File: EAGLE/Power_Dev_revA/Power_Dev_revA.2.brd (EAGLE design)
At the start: 63.5 x 31.8 mm, 36 parts, among them J5 MICRO_USB_SMD, Q1 SI2301CDS-T1-GE3, Q2 SI2301CDS-T1-GE3, U1 CN3791, U2 DW01A-G, U4 FS8205A

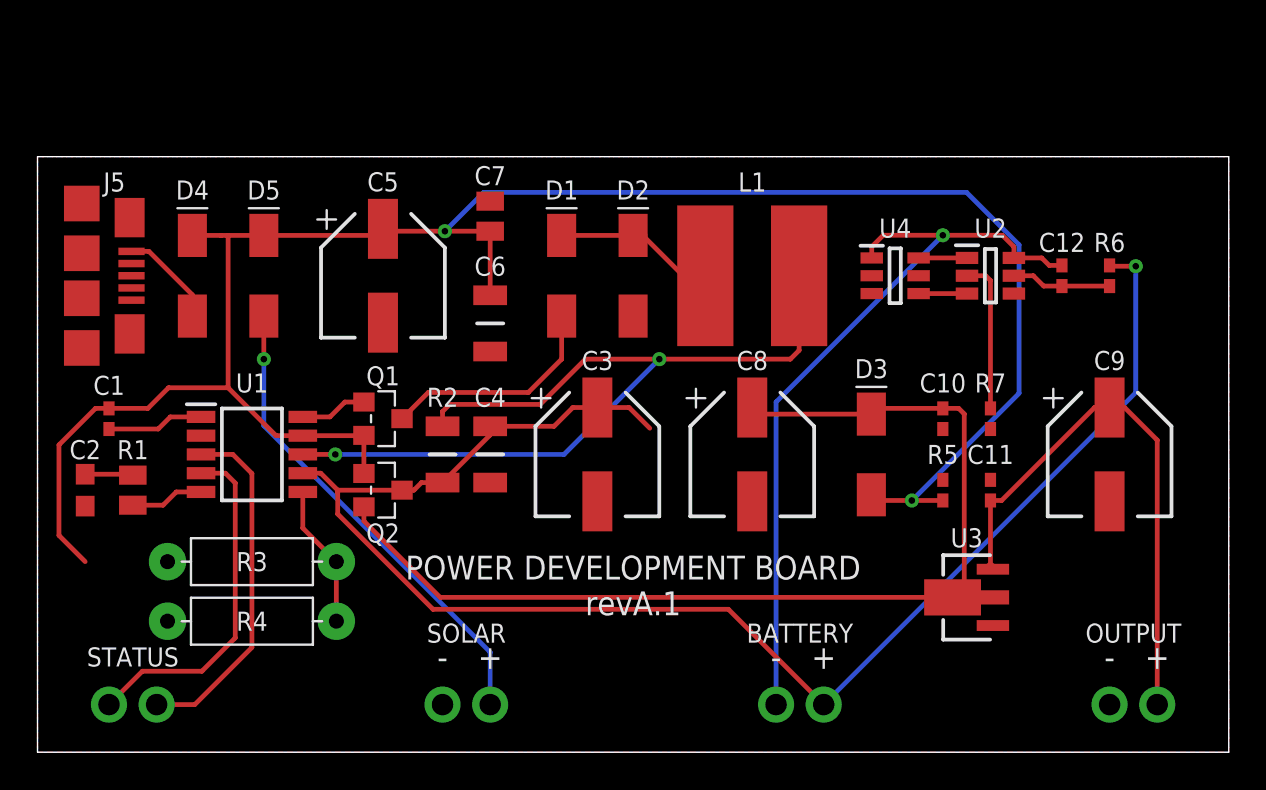
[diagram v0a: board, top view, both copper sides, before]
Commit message: Power A.2
Added connector for battery
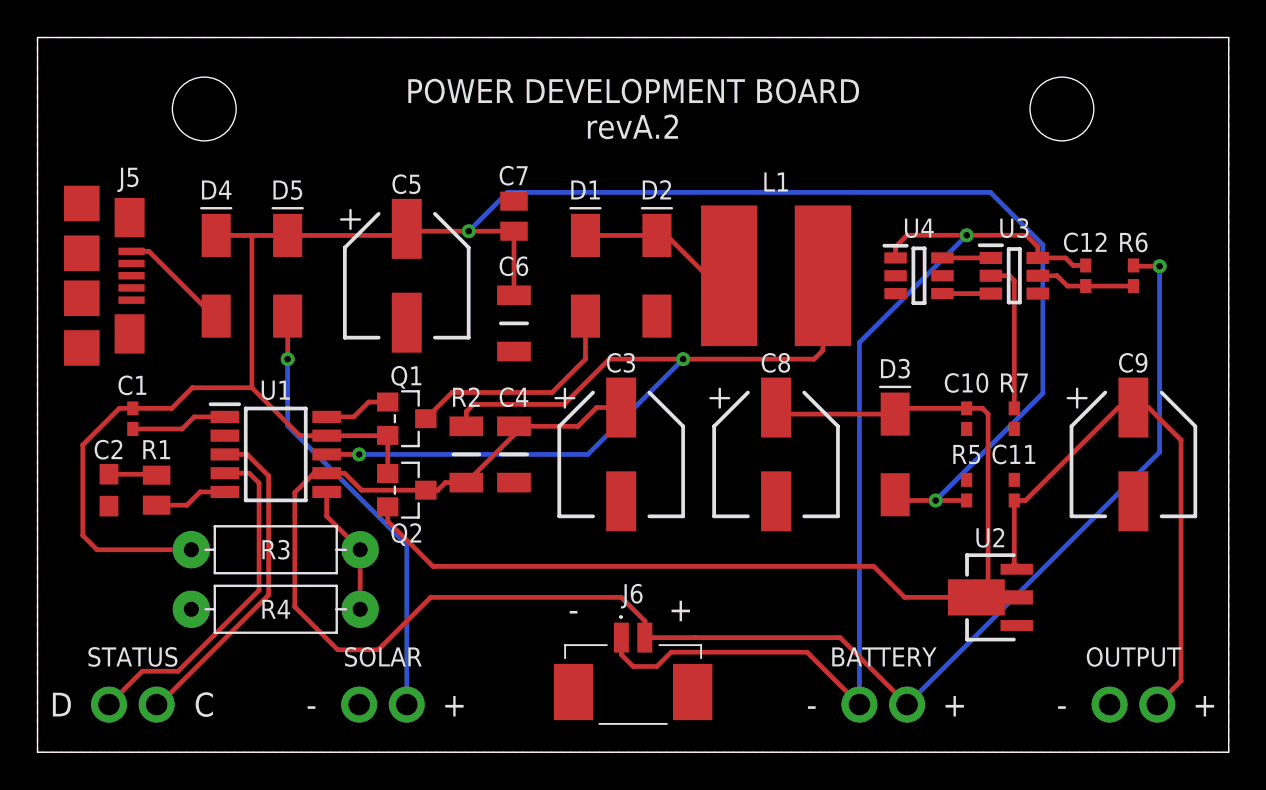
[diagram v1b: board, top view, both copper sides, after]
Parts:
- added J6: 53261-0271, NSE LABS:532610271
- U2: value DW01A-G -> (none); device NSE LABS:SOT95P280X135-6N -> NSE LABS:SOT-89-3
- U3: value (none) -> DW01A-G; device NSE LABS:SOT-89-3 -> NSE LABS:SOT95P280X135-6N
- moved U3 17.3 mm to (52.1, 25.4), turned to 0 degrees
- moved U2 17.1 mm to (50.8, 8.26), turned to 90 degrees
- moved BATTERY 4.45 mm to (45.1, 2.54)
- moved SOLAR 4.45 mm to (18.4, 2.54)
- moved R3 1.42 mm to (12.7, 10.8)
- moved R4 1.42 mm to (12.7, 7.62)
- moved C10 1.27 mm to (49.5, 17.8)
- moved C11 1.27 mm to (52.1, 14.0)
- moved C12 1.27 mm to (55.9, 25.4)
- moved C9 1.27 mm to (58.4, 15.9)
- moved D2 1.27 mm to (33.0, 25.4)
- moved R5 1.27 mm to (49.5, 14.0)
- moved R6 1.27 mm to (58.4, 25.4)
- moved R7 1.27 mm to (52.1, 17.8)
- moved U4 1.27 mm to (47.0, 25.4)
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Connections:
- net GND: now also U2.1; no longer U3.1
- net N$15: now also U3.2; no longer U2.2
- net N$16: now also U3.3; no longer U2.3
- net N$17: now also U3.1; no longer U2.1
- net N$18: now also J6.1, U3.6; no longer U2.6
- net N$19: now also U3.5; no longer U2.5
- net N$20: now also J6.2
- net N$6: now also U2.3; no longer U3.3
- net N$8: now also U2.2, U2.4; no longer U3.2, U3.4
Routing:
- net N$18: track 40.7 -> 54.7 mm
- net N$20: track 84.5 -> 94.4 mm
- net VDC: track 107.6 -> 111.7 mm
- net N$2: track 25.7 -> 23.3 mm
- net N$11: track 18.7 -> 17.5 mm
- net N$14: track 7.63 -> 7.00 mm
- net N$1: track 5.34 -> 5.94 mm
- net N$6: track 29.5 -> 30.0 mm
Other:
- board size 63.5 x 31.8 mm -> 63.5 x 38.1 mm
- board text added: "C"
- board text added: "D"
- board text added: "NSE LABS"
- board text added: "POWER DEVELOPMENT BOARD revA.2"
- board text removed: "POWER DEVELOPMENT BOARD revA.1"

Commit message: Power Board revision
Fixed error on MOSFET footprint and adjusted battery connector position in CPL file
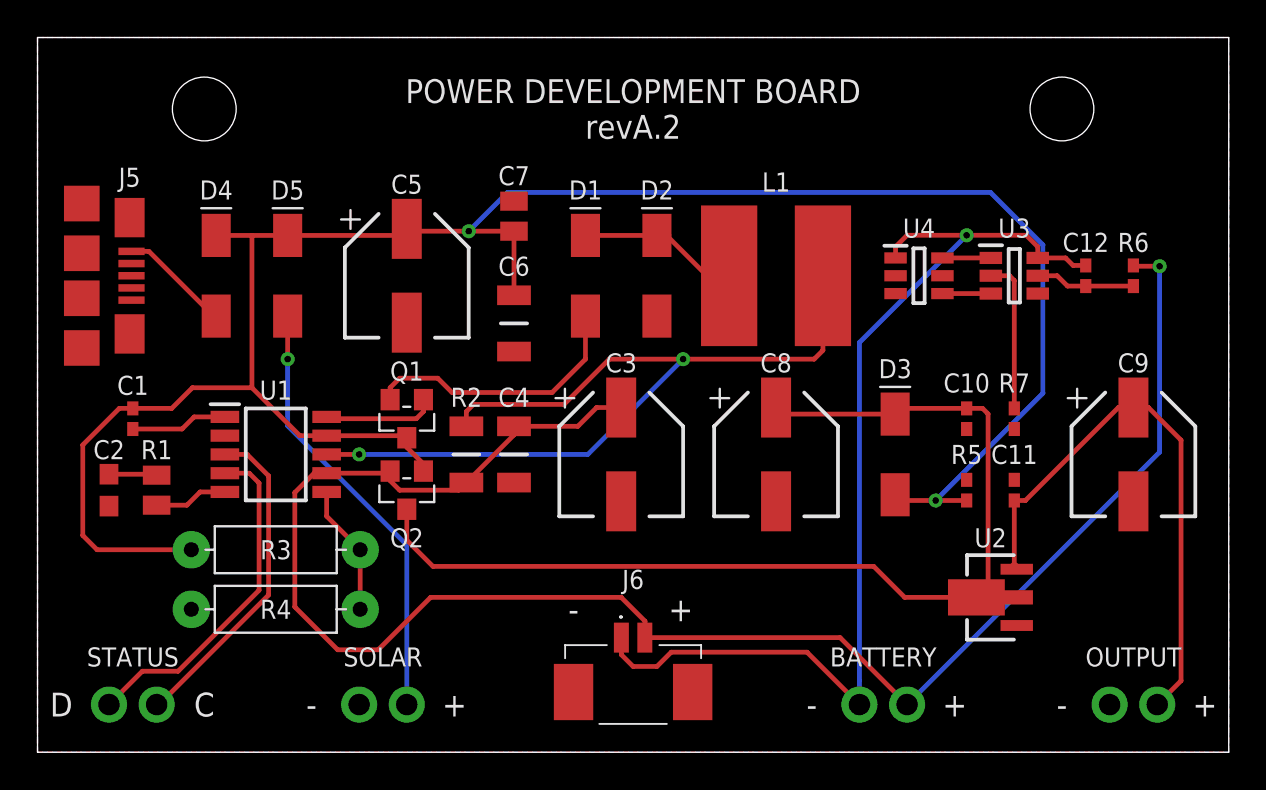
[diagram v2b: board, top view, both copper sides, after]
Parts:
- moved J6 0.76 mm to (31.8, 4.57)
- turned Q1 to 180 degrees
- turned Q2 to 180 degrees
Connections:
- net N$20: now also Q2.2; no longer Q2.3
- net N$3: now also Q1.2; no longer Q1.3
- net N$8: now also Q2.3; no longer Q2.2
- net VDC: now also Q1.3; no longer Q1.2
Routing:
- net N$3: track 12.1 -> 14.6 mm
- net N$7: track 3.59 -> 5.99 mm
- net VDC: track 111.7 -> 112.9 mm
- net N$8: track 57.9 -> 57.3 mm
